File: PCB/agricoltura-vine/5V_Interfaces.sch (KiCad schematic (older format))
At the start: 26 parts, among them K1 G5LE-14_DC5, K2 G5LE-14_DC5, Q1 IRLML6346TRPBF, Q2 IRLML6346TRPBF, T19 TSW-108-07-G-T, T20 0010897080, T22 0395121006, U10 ZXGD3009E6TA, U8 TCA6416ARTWR, U9 ZXGD3009E6TA

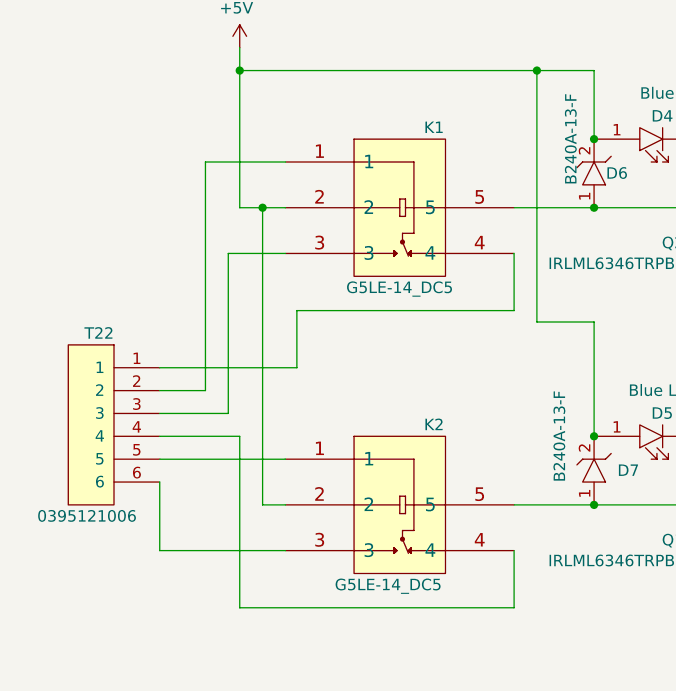
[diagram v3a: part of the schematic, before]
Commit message: Connector Swap
Switched over to dedicated connectors per relay
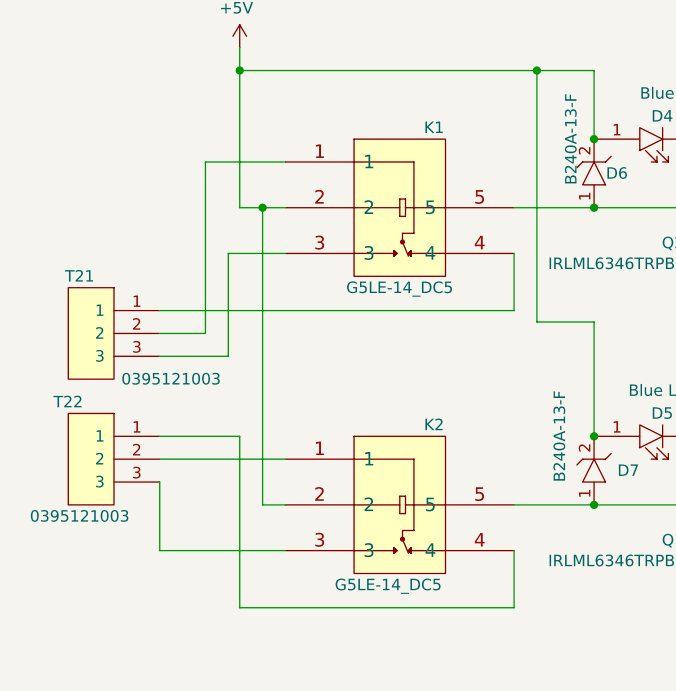
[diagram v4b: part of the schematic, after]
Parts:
- removed T22: 0395121006, AVR-KiCAD-Lib-Connectors:0395121006, symbol AVR-KiCAD-Lib-Connectors:0395121006
- added T21, T22: 0395121003, AVR-KiCAD-Lib-Connectors:0395121003, symbol AVR-KiCAD-Lib-Connectors:0395121003
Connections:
- wire segments 106 -> 104
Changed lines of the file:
@@
 	9050 6000 9050 6200
-$Comp
-L AVR-KiCAD-Lib-Connectors:0395121006 T22
-U 1 1 5F0AD388
-P 1250 3250
-F 0 "T22" H 1250 3400 50  0000 L CNN
-F 1 "0395121006" H 1150 2600 50  0000 L CNN
-F 2 "AVR-KiCAD-Lib-Connectors:0395121006" H 300 4300 50  0001 C CNN
-F 3 "https://www.molex.com/pdm_docs/sd/395121002_sd.pdf" H 1150 3350 50  0001 C CNN
-F 4 "1.79000" H 1350 3500 50  0001 C CNN "Cost QTY: 1"
-F 5 "0.79750" H 1450 3600 50  0001 C CNN "Cost QTY: 1000"
-F 6 "*" H 1550 3700 50  0001 C CNN "Cost QTY: 2500"
-F 7 "0.70125" H 1650 3800 50  0001 C CNN "Cost QTY: 5000"
-F 8 "*" H 1750 3900 50  0001 C CNN "Cost QTY: 10000"
-F 9 "Molex" H 1850 4000 50  0001 C CNN "MFR"
-F 10 "0395121006" H 1950 4100 50  0001 C CNN "MFR#"
-F 11 "Digikey" H 2050 4200 50  0001 C CNN "Vendor"
-F 12 "WM20088-ND" H 2150 4300 50  0001 C CNN "Vendor #"
-F 13 "AVR" H 2250 4400 50  0001 C CNN "Designer"
-F 14 "6.86mm" H 2350 4500 50  0001 C CNN "Height"
-F 15 "6/23/2020" H 3450 5600 50  0001 C CNN "Date Created"
-F 16 "6/23/2020" H 2450 4600 50  0001 C CNN "Date Modified"
-F 17 "Yes" H 2550 4700 50  0001 C CNN "Lead-Free ?"
-F 18 "1" H 2650 4800 50  0001 C CNN "RoHS Levels"
-F 19 "ThroughHole" H 2750 4900 50  0001 C CNN "Mounting"
-F 20 "6" H 2850 5000 50  0001 C CNN "Pin Count #"
-F 21 "Active" H 2950 5100 50  0001 C CNN "Status"
-F 22 "*" H 3050 5200 50  0001 C CNN "Tolerance"
-F 23 "Connector" H 3150 5300 50  0001 C CNN "Type"
-F 24 "300V" H 3250 5400 50  0001 C CNN "Voltage"
-F 25 "*" H 3350 5550 50  0001 C CNN "Package"
-F 26 "6 Position Terminal Block Header, Male Pins, Shrouded (4 Side) 0.150\" (3.81mm) 90°, Right Angle  Through Hole" H 3750 5950 50  0001 C CNN "Description"
-F 27 "0395121006" H 3550 5750 50  0001 C CNN "_Value_"
-F 28 "*" H 3650 5850 50  0001 C CNN "Management_ID"
-	1    1250 3250
-	-1   0    0    -1
-$EndComp
 $Comp
 L AVR-KiCAD-Lib-Mech-Relays-Contactors:G5LE-14_DC5 K2
@@
 	2000 2350 1650 2350
 Wire Wire Line
-	1650 2350 1650 3350
-Wire Wire Line
-	1650 3350 1450 3350
-Wire Wire Line
-	1450 3250 2050 3250
-Wire Wire Line
-	2050 3250 2050 3000
-Wire Wire Line
-	2050 3000 3000 3000
+	1650 2350 1650 3100
+Wire Wire Line
+	1650 3100 1450 3100
 Wire Wire Line
 	3000 3000 3000 2750
@@
 	2000 2750 1750 2750
 Wire Wire Line
-	1750 2750 1750 3450
-Wire Wire Line
-	1750 3450 1450 3450
+	1750 2750 1750 3200
+Wire Wire Line
+	1750 3200 1450 3200
 Wire Wire Line
 	9050 5900 9050 6000
@@
 Wire Wire Line
 	2600 6000 2600 6700
+$Comp
+L AVR-KiCAD-Lib-Connectors:0395121003 T21
+U 1 1 5EFF0D11
+P 1250 3000
+F 0 "T21" H 1400 3150 50  0000 C CNN
+F 1 "0395121003" H 1000 2700 50  0000 C CNN
+F 2 "AVR-KiCAD-Lib-Connectors:0395121003" H 300 4050 50  0001 C CNN
+F 3 "https://www.molex.com/pdm_docs/sd/395121002_sd.pdf" H 1150 3100 50  0001 C CNN
+F 4 "1.03000" H 1350 3250 50  0001 C CNN "Cost QTY: 1"
+F 5 "0.43200" H 1450 3350 50  0001 C CNN "Cost QTY: 1000"
+F 6 "*" H 1550 3450 50  0001 C CNN "Cost QTY: 2500"
+F 7 "0.35100" H 1650 3550 50  0001 C CNN "Cost QTY: 5000"
+F 8 "*" H 1750 3650 50  0001 C CNN "Cost QTY: 10000"
+F 9 "Molex" H 1850 3750 50  0001 C CNN "MFR"
+F 10 "0395121003" H 1950 3850 50  0001 C CNN "MFR#"
+F 11 "Digikey" H 2050 3950 50  0001 C CNN "Vendor"
+F 12 "WM20086-ND" H 2150 4050 50  0001 C CNN "Vendor #"
+F 13 "AVR" H 2250 4150 50  0001 C CNN "Designer"
+F 14 "6.86mm" H 2350 4250 50  0001 C CNN "Height"
+F 15 "7/2/2020" H 3450 5350 50  0001 C CNN "Date Created"
+F 16 "7/2/2020" H 2450 4350 50  0001 C CNN "Date Modified"
+F 17 "Yes" H 2550 4450 50  0001 C CNN "Lead-Free ?"
+F 18 "1" H 2650 4550 50  0001 C CNN "RoHS Levels"
+F 19 "ThroughHole" H 2750 4650 50  0001 C CNN "Mounting"
+F 20 "3" H 2850 4750 50  0001 C CNN "Pin Count #"
+F 21 "Active" H 2950 4850 50  0001 C CNN "Status"
+F 22 "*" H 3050 4950 50  0001 C CNN "Tolerance"
+F 23 "Connector" H 3150 5050 50  0001 C CNN "Type"
+F 24 "300V" H 3250 5150 50  0001 C CNN "Voltage"
+F 25 "*" H 3350 5300 50  0001 C CNN "Package"
+F 26 "3 Position Terminal Block Header, Male Pins, Shrouded (4 Side) 0.150\" (3.81mm) 90°, Right Angle  Through Hole" H 3750 5700 50  0001 C CNN "Description"
+F 27 "0395121003" H 3550 5500 50  0001 C CNN "_Value_"
+F 28 "*" H 3650 5600 50  0001 C CNN "Management_ID"
+	1    1250 3000
+	-1   0    0    -1
+$EndComp
+Wire Wire Line
+	1450 3000 3000 3000
+$Comp
+L AVR-KiCAD-Lib-Connectors:0395121003 T22
+U 1 1 5F0012A2
+P 1250 3550
+F 0 "T22" H 1450 3700 50  0000 C CNN
+F 1 "0395121003" H 1400 3200 50  0000 C CNN
+F 2 "AVR-KiCAD-Lib-Connectors:0395121003" H 300 4600 50  0001 C CNN
+F 3 "https://www.molex.com/pdm_docs/sd/395121002_sd.pdf" H 1150 3650 50  0001 C CNN
+F 4 "1.03000" H 1350 3800 50  0001 C CNN "Cost QTY: 1"
+F 5 "0.43200" H 1450 3900 50  0001 C CNN "Cost QTY: 1000"
+F 6 "*" H 1550 4000 50  0001 C CNN "Cost QTY: 2500"
+F 7 "0.35100" H 1650 4100 50  0001 C CNN "Cost QTY: 5000"
+F 8 "*" H 1750 4200 50  0001 C CNN "Cost QTY: 10000"
+F 9 "Molex" H 1850 4300 50  0001 C CNN "MFR"
+F 10 "0395121003" H 1950 4400 50  0001 C CNN "MFR#"
+F 11 "Digikey" H 2050 4500 50  0001 C CNN "Vendor"
+F 12 "WM20086-ND" H 2150 4600 50  0001 C CNN "Vendor #"
+F 13 "AVR" H 2250 4700 50  0001 C CNN "Designer"
+F 14 "6.86mm" H 2350 4800 50  0001 C CNN "Height"
+F 15 "7/2/2020" H 3450 5900 50  0001 C CNN "Date Created"
+F 16 "7/2/2020" H 2450 4900 50  0001 C CNN "Date Modified"
+F 17 "Yes" H 2550 5000 50  0001 C CNN "Lead-Free ?"
+F 18 "1" H 2650 5100 50  0001 C CNN "RoHS Levels"
+F 19 "ThroughHole" H 2750 5200 50  0001 C CNN "Mounting"
+F 20 "3" H 2850 5300 50  0001 C CNN "Pin Count #"
+F 21 "Active" H 2950 5400 50  0001 C CNN "Status"
+F 22 "*" H 3050 5500 50  0001 C CNN "Tolerance"
+F 23 "Connector" H 3150 5600 50  0001 C CNN "Type"
+F 24 "300V" H 3250 5700 50  0001 C CNN "Voltage"
+F 25 "*" H 3350 5850 50  0001 C CNN "Package"
+F 26 "3 Position Terminal Block Header, Male Pins, Shrouded (4 Side) 0.150\" (3.81mm) 90°, Right Angle  Through Hole" H 3750 6250 50  0001 C CNN "Description"
+F 27 "0395121003" H 3550 6050 50  0001 C CNN "_Value_"
+F 28 "*" H 3650 6150 50  0001 C CNN "Management_ID"
+	1    1250 3550
+	-1   0    0    -1
+$EndComp
 $EndSCHEMATC

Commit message: TVS Diodes
TVS diodes and pullups added to sensor connectors, implemented in schematic and board.
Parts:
- R19, R20, R21, R22: symbol AVR-KiCAD-Lib-Diodes:RC0402FR-0710RL -> agricoltura-vine-rescue:RC0402FR-0710RL-AVR-KiCAD-Lib-Diodes
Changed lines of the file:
@@
 $EndComp
 $Comp
-L AVR-KiCAD-Lib-Diodes:RC0402FR-0710RL R20
+L agricoltura-vine-rescue:RC0402FR-0710RL-AVR-KiCAD-Lib-Diodes R20
 U 1 1 5F210982
 P 4350 2750
+AR Path="/5F210982" Ref="R20"  Part="1"
+AR Path="/5EF943A9/5F210982" Ref="R20"  Part="1"
 F 0 "R20" H 4350 2850 50  0000 C CNN
 F 1 "RC0402FR-0710RL" H 4350 2975 50  0001 C CNN
@@
 Connection ~ 4150 2750
 $Comp
-L AVR-KiCAD-Lib-Diodes:RC0402FR-0710RL R19
+L agricoltura-vine-rescue:RC0402FR-0710RL-AVR-KiCAD-Lib-Diodes R19
 U 1 1 5F2245B4
 P 4350 2450
+AR Path="/5F2245B4" Ref="R19"  Part="1"
+AR Path="/5EF943A9/5F2245B4" Ref="R19"  Part="1"
 F 0 "R19" H 4350 2550 50  0000 C CNN
 F 1 "RC0402FR-0710RL" H 4350 2675 50  0001 C CNN
@@
 $EndComp
 $Comp
-L AVR-KiCAD-Lib-Diodes:RC0402FR-0710RL R22
+L agricoltura-vine-rescue:RC0402FR-0710RL-AVR-KiCAD-Lib-Diodes R22
 U 1 1 5F22EE9F
 P 4350 4050
+AR Path="/5F22EE9F" Ref="R22"  Part="1"
+AR Path="/5EF943A9/5F22EE9F" Ref="R22"  Part="1"
 F 0 "R22" H 4350 4150 50  0000 C CNN
 F 1 "RC0402FR-0710RL" H 4350 4275 50  0001 C CNN
@@
 Connection ~ 4150 4050
 $Comp
-L AVR-KiCAD-Lib-Diodes:RC0402FR-0710RL R21
+L agricoltura-vine-rescue:RC0402FR-0710RL-AVR-KiCAD-Lib-Diodes R21
 U 1 1 5F22EEC0
 P 4350 3750
+AR Path="/5F22EEC0" Ref="R21"  Part="1"
+AR Path="/5EF943A9/5F22EEC0" Ref="R21"  Part="1"
 F 0 "R21" H 4350 3850 50  0000 C CNN
 F 1 "RC0402FR-0710RL" H 4350 3975 50  0001 C CNN
